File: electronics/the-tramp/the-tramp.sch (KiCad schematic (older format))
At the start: 14 parts

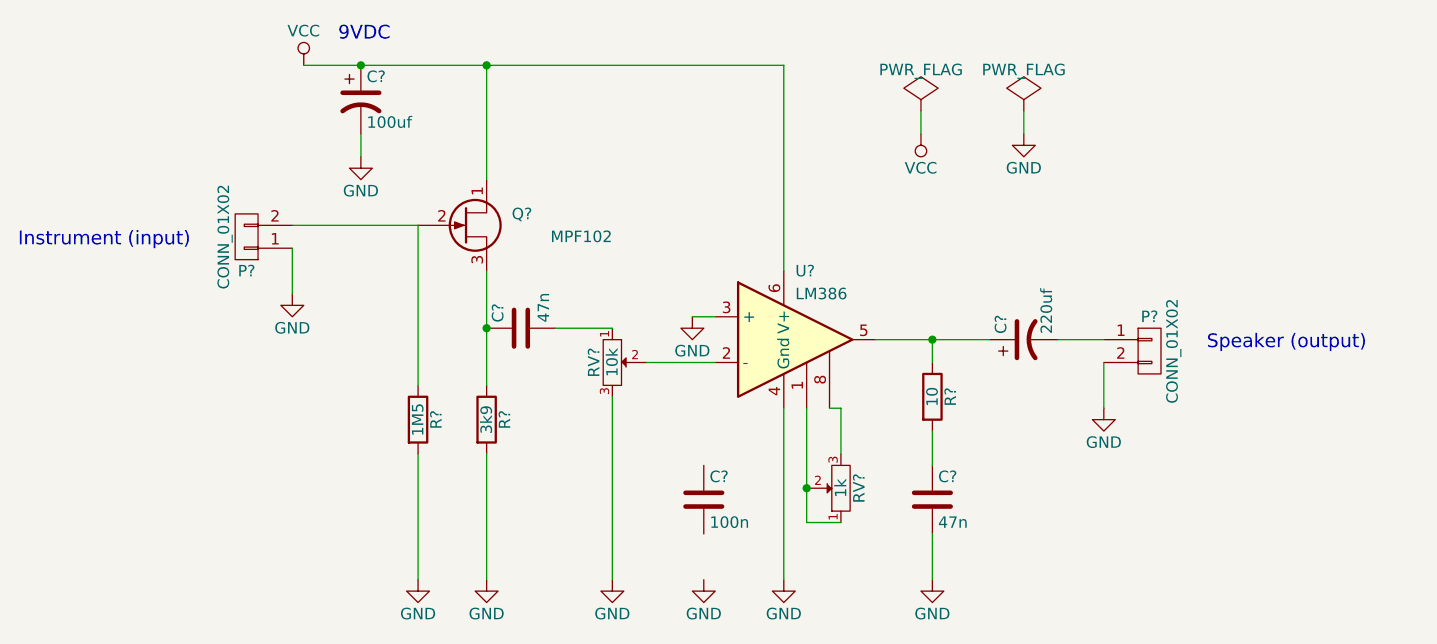
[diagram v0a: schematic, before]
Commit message: Made a custom LM386 that includes pin 7.
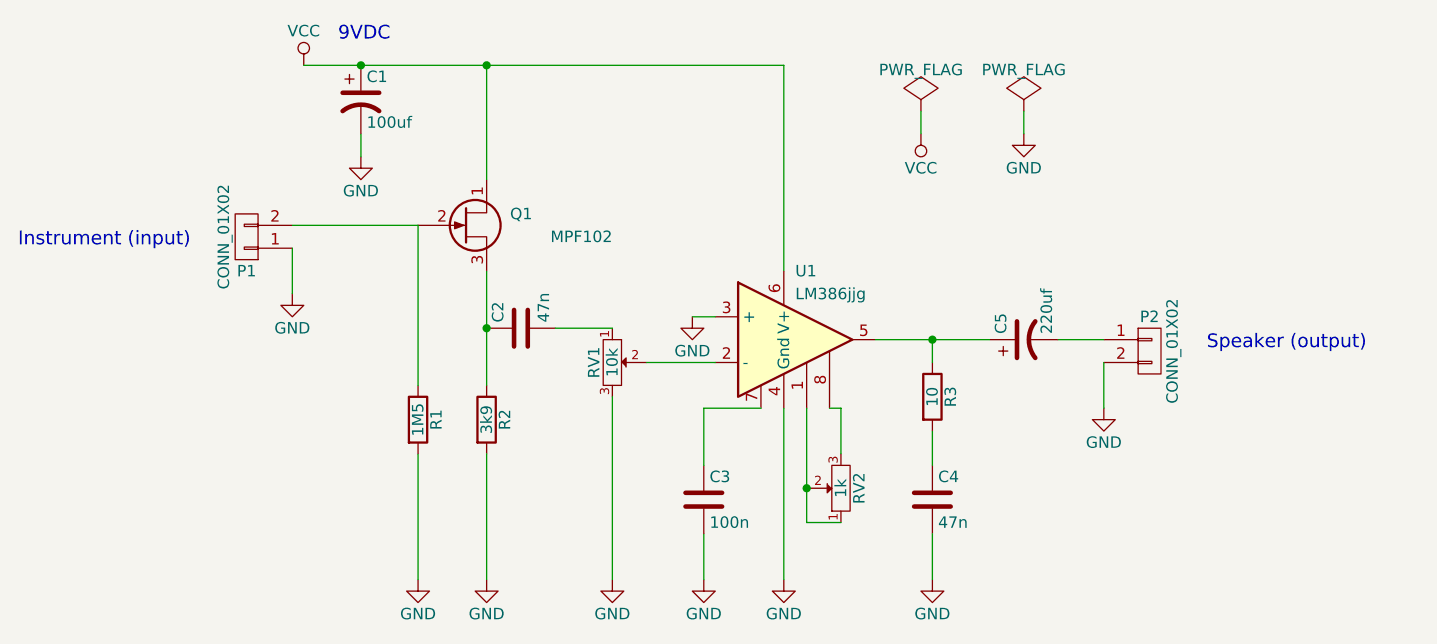
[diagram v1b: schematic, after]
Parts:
- removed U?: LM386, symbol LM386
- added U1: LM386jjg, symbol LM386jjg
- gave numbers to parts that had none: 13
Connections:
- net GND: now also C3.2, U1.3 (+), U1.4 (Gnd)
- net VCC: now also U1.6 (V+)
- net at RV2.1, RV2.2: now also U1.1
- net at RV1.2: now also U1.2 (-)
- net at C5.1, R3.1: now also U1.5
- net at RV2.3: now also U1.8
- net at C3.1: now also U1.7
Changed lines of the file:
@@
 LIBS:contrib
 LIBS:valves
-LIBS:myLib
+LIBS:tramp
 LIBS:the-tramp-cache
 EELAYER 25 0
@@
 $EndDescr
 $Comp
-L CP1 C?
+L CP1 C5
 U 1 1 5AD9FF9B
 P 6400 3700
-F 0 "C?" H 6425 3800 50  0000 L CNN
+F 0 "C5" H 6425 3800 50  0000 L CNN
 F 1 "220uf" H 6425 3600 50  0000 L CNN
 F 2 "" H 6400 3700 50  0000 C CNN
@@
 $EndComp
 $Comp
-L CP1 C?
+L CP1 C1
 U 1 1 5AD9FFC6
 P 3500 2650
-F 0 "C?" H 3525 2750 50  0000 L CNN
+F 0 "C1" H 3525 2750 50  0000 L CNN
 F 1 "100uf" H 3525 2550 50  0000 L CNN
 F 2 "" H 3500 2650 50  0000 C CNN
@@
 $EndComp
 $Comp
-L C C?
+L C C2
 U 1 1 5ADA00BD
 P 4200 3650
-F 0 "C?" H 4225 3750 50  0000 L CNN
+F 0 "C2" H 4225 3750 50  0000 L CNN
 F 1 "47n" H 4225 3550 50  0000 L CNN
 F 2 "" H 4238 3500 50  0000 C CNN
@@
 $EndComp
 $Comp
-L R R?
+L R R3
 U 1 1 5ADA0106
 P 6000 3950
-F 0 "R?" V 6080 3950 50  0000 C CNN
+F 0 "R3" V 6080 3950 50  0000 C CNN
 F 1 "10" V 6000 3950 50  0000 C CNN
 F 2 "" V 5930 3950 50  0000 C CNN
@@
 $EndComp
 $Comp
-L R R?
+L R R2
 U 1 1 5ADA0142
 P 4050 4050
-F 0 "R?" V 4130 4050 50  0000 C CNN
+F 0 "R2" V 4130 4050 50  0000 C CNN
 F 1 "3k9" V 4050 4050 50  0000 C CNN
 F 2 "" V 3980 4050 50  0000 C CNN
@@
 $EndComp
 $Comp
-L R R?
+L R R1
 U 1 1 5ADA01A6
 P 3750 4050
-F 0 "R?" V 3830 4050 50  0000 C CNN
+F 0 "R1" V 3830 4050 50  0000 C CNN
 F 1 "1M5" V 3750 4050 50  0000 C CNN
 F 2 "" V 3680 4050 50  0000 C CNN
@@
 $EndComp
 $Comp
-L POT RV?
+L POT RV1
 U 1 1 5ADA01D4
 P 4600 3800
-F 0 "RV?" H 4600 3720 50  0000 C CNN
+F 0 "RV1" H 4600 3720 50  0000 C CNN
 F 1 "10k" H 4600 3800 50  0000 C CNN
 F 2 "" H 4600 3800 50  0000 C CNN
@@
 $EndComp
 $Comp
-L POT RV?
+L POT RV2
 U 1 1 5ADA0201
 P 5600 4350
-F 0 "RV?" H 5600 4270 50  0000 C CNN
+F 0 "RV2" H 5600 4270 50  0000 C CNN
 F 1 "1k" H 5600 4350 50  0000 C CNN
 F 2 "" H 5600 4350 50  0000 C CNN
@@
 $EndComp
 $Comp
-L C C?
+L C C3
 U 1 1 5ADA025A
 P 5000 4400
-F 0 "C?" H 5025 4500 50  0000 L CNN
+F 0 "C3" H 5025 4500 50  0000 L CNN
 F 1 "100n" H 5025 4300 50  0000 L CNN
 F 2 "" H 5038 4250 50  0000 C CNN
@@
 $EndComp
 $Comp
-L Q_NJFET_DGS Q?
+L Q_NJFET_DGS Q1
 U 1 1 5ADA02C2
 P 3950 3200
-F 0 "Q?" H 4250 3250 50  0000 R CNN
+F 0 "Q1" H 4250 3250 50  0000 R CNN
 F 1 "MPF102" H 4600 3150 50  0000 R CNN
 F 2 "" H 4150 3300 50  0000 C CNN
@@
 $EndComp
 $Comp
-L C C?
+L C C4
 U 1 1 5ADA0C34
 P 6000 4400
-F 0 "C?" H 6025 4500 50  0000 L CNN
+F 0 "C4" H 6025 4500 50  0000 L CNN
 F 1 "47n" H 6025 4300 50  0000 L CNN
 F 2 "" H 6038 4250 50  0000 C CNN
@@
 $EndComp
 $Comp
-L VCC #PWR?
+L VCC #PWR2
 U 1 1 5ADA17B8
 P 3250 2500
-F 0 "#PWR?" H 3250 2350 50  0001 C CNN
+F 0 "#PWR2" H 3250 2350 50  0001 C CNN
 F 1 "VCC" H 3250 2650 50  0000 C CNN
 F 2 "" H 3250 2500 50  0000 C CNN
@@
 $EndComp
 $Comp
-L GND #PWR?
+L GND #PWR4
 U 1 1 5ADA17E4
 P 3750 4750
-F 0 "#PWR?" H 3750 4500 50  0001 C CNN
+F 0 "#PWR4" H 3750 4500 50  0001 C CNN
 F 1 "GND" H 3750 4600 50  0000 C CNN
 F 2 "" H 3750 4750 50  0000 C CNN
@@
 $EndComp
 $Comp
-L GND #PWR?
+L GND #PWR5
 U 1 1 5ADA181A
 P 4050 4750
-F 0 "#PWR?" H 4050 4500 50  0001 C CNN
+F 0 "#PWR5" H 4050 4500 50  0001 C CNN
 F 1 "GND" H 4050 4600 50  0000 C CNN
 F 2 "" H 4050 4750 50  0000 C CNN
@@
 $EndComp
 $Comp
-L GND #PWR?
+L GND #PWR8
 U 1 1 5ADA1849
 P 5000 4750
-F 0 "#PWR?" H 5000 4500 50  0001 C CNN
+F 0 "#PWR8" H 5000 4500 50  0001 C CNN
 F 1 "GND" H 5000 4600 50  0000 C CNN
 F 2 "" H 5000 4750 50  0000 C CNN
@@
 $EndComp
 $Comp
-L GND #PWR?
+L GND #PWR9
 U 1 1 5ADA1AB8
 P 5350 4750
-F 0 "#PWR?" H 5350 4500 50  0001 C CNN
+F 0 "#PWR9" H 5350 4500 50  0001 C CNN
 F 1 "GND" H 5350 4600 50  0000 C CNN
 F 2 "" H 5350 4750 50  0000 C CNN
@@
 $EndComp
 $Comp
-L GND #PWR?
+L GND #PWR11
 U 1 1 5ADA1AE7
 P 6000 4750
-F 0 "#PWR?" H 6000 4500 50  0001 C CNN
+F 0 "#PWR11" H 6000 4500 50  0001 C CNN
 F 1 "GND" H 6000 4600 50  0000 C CNN
 F 2 "" H 6000 4750 50  0000 C CNN
@@
 $EndComp
 $Comp
-L GND #PWR?
+L GND #PWR13
 U 1 1 5ADA1B16
 P 6750 4000
-F 0 "#PWR?" H 6750 3750 50  0001 C CNN
+F 0 "#PWR13" H 6750 3750 50  0001 C CNN
 F 1 "GND" H 6750 3850 50  0000 C CNN
 F 2 "" H 6750 4000 50  0000 C CNN
@@
 $EndComp
 $Comp
-L GND #PWR?
+L GND #PWR3
 U 1 1 5ADA1DC1
 P 3500 2900
-F 0 "#PWR?" H 3500 2650 50  0001 C CNN
+F 0 "#PWR3" H 3500 2650 50  0001 C CNN
 F 1 "GND" H 3500 2750 50  0000 C CNN
 F 2 "" H 3500 2900 50  0000 C CNN
@@
 	5050 3800 4750 3800
 $Comp
-L GND #PWR?
+L GND #PWR7
 U 1 1 5ADA210E
 P 4950 3600
-F 0 "#PWR?" H 4950 3350 50  0001 C CNN
+F 0 "#PWR7" H 4950 3350 50  0001 C CNN
 F 1 "GND" H 4950 3450 50  0000 C CNN
 F 2 "" H 4950 3600 50  0000 C CNN
@@
 	4600 3650 4350 3650
 Wire Wire Line
-	4050 3400 4050 3650
-Wire Wire Line
-	4050 3650 4050 3900
+	4050 3400 4050 3900
 Connection ~ 4050 3650
 Wire Wire Line
 	4050 4200 4050 4750
 $Comp
-L GND #PWR?
+L GND #PWR6
 U 1 1 5ADA2193
 P 4600 4750
-F 0 "#PWR?" H 4600 4500 50  0001 C CNN
+F 0 "#PWR6" H 4600 4500 50  0001 C CNN
 F 1 "GND" H 4600 4600 50  0000 C CNN
 F 2 "" H 4600 4750 50  0000 C CNN
@@
 	5350 2500 5350 3400
 Wire Wire Line
-	3250 2500 3500 2500
-Wire Wire Line
-	3500 2500 4050 2500
-Wire Wire Line
-	4050 2500 5350 2500
+	3250 2500 5350 2500
 Connection ~ 3500 2500
 Wire Wire Line
@@
 	3500 2800 3500 2900
 Wire Wire Line
-	5750 3700 6000 3700
-Wire Wire Line
-	6000 3700 6250 3700
+	5750 3700 6250 3700
 Wire Wire Line
 	6000 3800 6000 3700
@@
 	6000 4550 6000 4750
 Wire Wire Line
-	5450 4000 5450 4350
-Wire Wire Line
-	5450 4350 5450 4500
+	5450 4000 5450 4500
 Wire Wire Line
 	5450 4500 5600 4500
@@
 	5350 4000 5350 4750
 $Comp
-L CONN_01X02 P?
+L CONN_01X02 P2
 U 1 1 5ADA31D0
 P 6950 3750
-F 0 "P?" H 6950 3900 50  0000 C CNN
+F 0 "P2" H 6950 3900 50  0000 C CNN
 F 1 "CONN_01X02" V 7050 3750 50  0000 C CNN
 F 2 "" H 6950 3750 50  0000 C CNN
@@
 	6750 3800 6750 4000
 $Comp
-L CONN_01X02 P?
+L CONN_01X02 P1
 U 1 1 5ADA38CB
 P 3000 3250
-F 0 "P?" H 3000 3400 50  0000 C CNN
+F 0 "P1" H 3000 3400 50  0000 C CNN
 F 1 "CONN_01X02" V 3100 3250 50  0000 C CNN
 F 2 "" H 3000 3250 50  0000 C CNN
@@
 $EndComp
 $Comp
-L GND #PWR?
+L GND #PWR1
 U 1 1 5ADA3A4A
 P 3200 3500
-F 0 "#PWR?" H 3200 3250 50  0001 C CNN
+F 0 "#PWR1" H 3200 3250 50  0001 C CNN
 F 1 "GND" H 3200 3350 50  0000 C CNN
 F 2 "" H 3200 3500 50  0000 C CNN
@@
 	3200 3300 3200 3500
 $Comp
-L PWR_FLAG #FLG?
+L PWR_FLAG #FLG1
 U 1 1 5ADA4A9D
 P 5950 2700
-F 0 "#FLG?" H 5950 2795 50  0001 C CNN
+F 0 "#FLG1" H 5950 2795 50  0001 C CNN
 F 1 "PWR_FLAG" H 5950 2880 50  0000 C CNN
 F 2 "" H 5950 2700 50  0000 C CNN
@@
 $EndComp
 $Comp
-L VCC #PWR?
+L VCC #PWR10
 U 1 1 5ADA4ACD
 P 5950 2800
-F 0 "#PWR?" H 5950 2650 50  0001 C CNN
+F 0 "#PWR10" H 5950 2650 50  0001 C CNN
 F 1 "VCC" H 5950 2950 50  0000 C CNN
 F 2 "" H 5950 2800 50  0000 C CNN
@@
 $EndComp
 $Comp
-L PWR_FLAG #FLG?
+L PWR_FLAG #FLG2
 U 1 1 5ADA4B60
 P 6400 2700
-F 0 "#FLG?" H 6400 2795 50  0001 C CNN
+F 0 "#FLG2" H 6400 2795 50  0001 C CNN
 F 1 "PWR_FLAG" H 6400 2880 50  0000 C CNN
 F 2 "" H 6400 2700 50  0000 C CNN
@@
 $EndComp
 $Comp
-L GND #PWR?
+L GND #PWR12
 U 1 1 5ADA4B95
 P 6400 2800
-F 0 "#PWR?" H 6400 2550 50  0001 C CNN
+F 0 "#PWR12" H 6400 2550 50  0001 C CNN
 F 1 "GND" H 6400 2650 50  0000 C CNN
 F 2 "" H 6400 2800 50  0000 C CNN
@@
 	5600 4000 5600 4200
 $Comp
-L LM386 U?
-U 1 1 5AD9FF41
+L LM386jjg U1
+U 1 1 5ADA290D
 P 5350 3700
-F 0 "U?" H 5400 4000 50  0000 L CNN
-F 1 "LM386" H 5400 3900 50  0000 L CNN
+F 0 "U1" H 5400 4000 50  0000 L CNN
+F 1 "LM386jjg" H 5400 3900 50  0000 L CNN
 F 2 "" H 5450 3800 50  0000 C CNN
 F 3 "" H 5550 3900 50  0000 C CNN
@@
 	1    0    0    -1
 $EndComp
+Wire Wire Line
+	5250 4000 5000 4000
+Wire Wire Line
+	5000 4000 5000 4250
+Wire Wire Line
+	5000 4550 5000 4750
 $EndSCHEMATC

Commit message: First run at laying out the board.
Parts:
- C1, C5: footprint (none) -> Capacitors_ThroughHole:C_Radial_D8_L11.5_P3.5
- C2, C3, C4: footprint (none) -> Capacitors_ThroughHole:C_Rect_L7.5_W6.5_P5
- P1, P2: footprint (none) -> Pin_Headers:Pin_Header_Straight_1x02
- Q1: footprint (none) -> TO_SOT_Packages_THT:TO-92_Inline_Wide
- R1, R2, R3: footprint (none) -> Discret:R3
- RV1, RV2: footprint (none) -> Potentiometers:Potentiometer_Alps-RK16-single_largePads
- U1: footprint (none) -> Housings_DIP:DIP-8_W7.62mm_LongPads
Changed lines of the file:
@@
 F 0 "C5" H 6425 3800 50  0000 L CNN
 F 1 "220uf" H 6425 3600 50  0000 L CNN
-F 2 "" H 6400 3700 50  0000 C CNN
+F 2 "Capacitors_ThroughHole:C_Radial_D8_L11.5_P3.5" H 6400 3700 50  0001 C CNN
 F 3 "" H 6400 3700 50  0000 C CNN
 	1    6400 3700
@@
 F 0 "C1" H 3525 2750 50  0000 L CNN
 F 1 "100uf" H 3525 2550 50  0000 L CNN
-F 2 "" H 3500 2650 50  0000 C CNN
+F 2 "Capacitors_ThroughHole:C_Radial_D8_L11.5_P3.5" H 3500 2650 50  0001 C CNN
 F 3 "" H 3500 2650 50  0000 C CNN
 	1    3500 2650
@@
 F 0 "C2" H 4225 3750 50  0000 L CNN
 F 1 "47n" H 4225 3550 50  0000 L CNN
-F 2 "" H 4238 3500 50  0000 C CNN
+F 2 "Capacitors_ThroughHole:C_Rect_L7.5_W6.5_P5" H 4238 3500 50  0001 C CNN
 F 3 "" H 4200 3650 50  0000 C CNN
 	1    4200 3650
@@
 F 0 "R3" V 6080 3950 50  0000 C CNN
 F 1 "10" V 6000 3950 50  0000 C CNN
-F 2 "" V 5930 3950 50  0000 C CNN
+F 2 "Discret:R3" V 5930 3950 50  0001 C CNN
 F 3 "" H 6000 3950 50  0000 C CNN
 	1    6000 3950
@@
 F 0 "R2" V 4130 4050 50  0000 C CNN
 F 1 "3k9" V 4050 4050 50  0000 C CNN
-F 2 "" V 3980 4050 50  0000 C CNN
+F 2 "Discret:R3" V 3980 4050 50  0001 C CNN
 F 3 "" H 4050 4050 50  0000 C CNN
 	1    4050 4050
@@
 F 0 "R1" V 3830 4050 50  0000 C CNN
 F 1 "1M5" V 3750 4050 50  0000 C CNN
-F 2 "" V 3680 4050 50  0000 C CNN
+F 2 "Discret:R3" V 3680 4050 50  0001 C CNN
 F 3 "" H 3750 4050 50  0000 C CNN
 	1    3750 4050
@@
 F 0 "RV1" H 4600 3720 50  0000 C CNN
 F 1 "10k" H 4600 3800 50  0000 C CNN
-F 2 "" H 4600 3800 50  0000 C CNN
+F 2 "Potentiometers:Potentiometer_Alps-RK16-single_largePads" H 4600 3800 50  0001 C CNN
 F 3 "" H 4600 3800 50  0000 C CNN
 	1    4600 3800
@@
 F 0 "RV2" H 5600 4270 50  0000 C CNN
 F 1 "1k" H 5600 4350 50  0000 C CNN
-F 2 "" H 5600 4350 50  0000 C CNN
+F 2 "Potentiometers:Potentiometer_Alps-RK16-single_largePads" H 5600 4350 50  0001 C CNN
 F 3 "" H 5600 4350 50  0000 C CNN
 	1    5600 4350
@@
 F 0 "C3" H 5025 4500 50  0000 L CNN
 F 1 "100n" H 5025 4300 50  0000 L CNN
-F 2 "" H 5038 4250 50  0000 C CNN
+F 2 "Capacitors_ThroughHole:C_Rect_L7.5_W6.5_P5" H 5038 4250 50  0001 C CNN
 F 3 "" H 5000 4400 50  0000 C CNN
 	1    5000 4400
@@
 F 0 "Q1" H 4250 3250 50  0000 R CNN
 F 1 "MPF102" H 4600 3150 50  0000 R CNN
-F 2 "" H 4150 3300 50  0000 C CNN
+F 2 "TO_SOT_Packages_THT:TO-92_Inline_Wide" H 4150 3300 50  0001 C CNN
 F 3 "" H 3950 3200 50  0000 C CNN
 	1    3950 3200
@@
 F 0 "C4" H 6025 4500 50  0000 L CNN
 F 1 "47n" H 6025 4300 50  0000 L CNN
-F 2 "" H 6038 4250 50  0000 C CNN
+F 2 "Capacitors_ThroughHole:C_Rect_L7.5_W6.5_P5" H 6038 4250 50  0001 C CNN
 F 3 "" H 6000 4400 50  0000 C CNN
 	1    6000 4400
@@
 $EndComp
 $Comp
-L VCC #PWR2
+L VCC #PWR01
 U 1 1 5ADA17B8
 P 3250 2500
-F 0 "#PWR2" H 3250 2350 50  0001 C CNN
+F 0 "#PWR01" H 3250 2350 50  0001 C CNN
 F 1 "VCC" H 3250 2650 50  0000 C CNN
 F 2 "" H 3250 2500 50  0000 C CNN
@@
 $EndComp
 $Comp
-L GND #PWR4
+L GND #PWR02
 U 1 1 5ADA17E4
 P 3750 4750
-F 0 "#PWR4" H 3750 4500 50  0001 C CNN
+F 0 "#PWR02" H 3750 4500 50  0001 C CNN
 F 1 "GND" H 3750 4600 50  0000 C CNN
 F 2 "" H 3750 4750 50  0000 C CNN
@@
 $EndComp
 $Comp
-L GND #PWR5
+L GND #PWR03
 U 1 1 5ADA181A
 P 4050 4750
-F 0 "#PWR5" H 4050 4500 50  0001 C CNN
+F 0 "#PWR03" H 4050 4500 50  0001 C CNN
 F 1 "GND" H 4050 4600 50  0000 C CNN
 F 2 "" H 4050 4750 50  0000 C CNN
@@
 $EndComp
 $Comp
-L GND #PWR8
+L GND #PWR04
 U 1 1 5ADA1849
 P 5000 4750
-F 0 "#PWR8" H 5000 4500 50  0001 C CNN
+F 0 "#PWR04" H 5000 4500 50  0001 C CNN
 F 1 "GND" H 5000 4600 50  0000 C CNN
 F 2 "" H 5000 4750 50  0000 C CNN
@@
 $EndComp
 $Comp
-L GND #PWR9
+L GND #PWR05
 U 1 1 5ADA1AB8
 P 5350 4750
-F 0 "#PWR9" H 5350 4500 50  0001 C CNN
+F 0 "#PWR05" H 5350 4500 50  0001 C CNN
 F 1 "GND" H 5350 4600 50  0000 C CNN
 F 2 "" H 5350 4750 50  0000 C CNN
@@
 $EndComp
 $Comp
-L GND #PWR11
+L GND #PWR06
 U 1 1 5ADA1AE7
 P 6000 4750
-F 0 "#PWR11" H 6000 4500 50  0001 C CNN
+F 0 "#PWR06" H 6000 4500 50  0001 C CNN
 F 1 "GND" H 6000 4600 50  0000 C CNN
 F 2 "" H 6000 4750 50  0000 C CNN
@@
 $EndComp
 $Comp
-L GND #PWR13
+L GND #PWR07
 U 1 1 5ADA1B16
 P 6750 4000
-F 0 "#PWR13" H 6750 3750 50  0001 C CNN
+F 0 "#PWR07" H 6750 3750 50  0001 C CNN
 F 1 "GND" H 6750 3850 50  0000 C CNN
 F 2 "" H 6750 4000 50  0000 C CNN
@@
 $EndComp
 $Comp
-L GND #PWR3
+L GND #PWR08
 U 1 1 5ADA1DC1
 P 3500 2900
-F 0 "#PWR3" H 3500 2650 50  0001 C CNN
+F 0 "#PWR08" H 3500 2650 50  0001 C CNN
 F 1 "GND" H 3500 2750 50  0000 C CNN
 F 2 "" H 3500 2900 50  0000 C CNN
@@
 	5050 3800 4750 3800
 $Comp
-L GND #PWR7
+L GND #PWR09
 U 1 1 5ADA210E
 P 4950 3600
-F 0 "#PWR7" H 4950 3350 50  0001 C CNN
+F 0 "#PWR09" H 4950 3350 50  0001 C CNN
 F 1 "GND" H 4950 3450 50  0000 C CNN
 F 2 "" H 4950 3600 50  0000 C CNN
@@
 	4050 4200 4050 4750
 $Comp
-L GND #PWR6
+L GND #PWR010
 U 1 1 5ADA2193
 P 4600 4750
-F 0 "#PWR6" H 4600 4500 50  0001 C CNN
+F 0 "#PWR010" H 4600 4500 50  0001 C CNN
 F 1 "GND" H 4600 4600 50  0000 C CNN
 F 2 "" H 4600 4750 50  0000 C CNN
@@
 F 0 "P2" H 6950 3900 50  0000 C CNN
 F 1 "CONN_01X02" V 7050 3750 50  0000 C CNN
-F 2 "" H 6950 3750 50  0000 C CNN
+F 2 "Pin_Headers:Pin_Header_Straight_1x02" H 6950 3750 50  0001 C CNN
 F 3 "" H 6950 3750 50  0000 C CNN
 	1    6950 3750
@@
 F 0 "P1" H 3000 3400 50  0000 C CNN
 F 1 "CONN_01X02" V 3100 3250 50  0000 C CNN
-F 2 "" H 3000 3250 50  0000 C CNN
+F 2 "Pin_Headers:Pin_Header_Straight_1x02" H 3000 3250 50  0001 C CNN
 F 3 "" H 3000 3250 50  0000 C CNN
 	1    3000 3250
@@
 $EndComp
 $Comp
-L GND #PWR1
+L GND #PWR011
 U 1 1 5ADA3A4A
 P 3200 3500
-F 0 "#PWR1" H 3200 3250 50  0001 C CNN
+F 0 "#PWR011" H 3200 3250 50  0001 C CNN
 F 1 "GND" H 3200 3350 50  0000 C CNN
 F 2 "" H 3200 3500 50  0000 C CNN
@@
 	3200 3300 3200 3500
 $Comp
-L PWR_FLAG #FLG1
+L PWR_FLAG #FLG012
 U 1 1 5ADA4A9D
 P 5950 2700
-F 0 "#FLG1" H 5950 2795 50  0001 C CNN
+F 0 "#FLG012" H 5950 2795 50  0001 C CNN
 F 1 "PWR_FLAG" H 5950 2880 50  0000 C CNN
 F 2 "" H 5950 2700 50  0000 C CNN
@@
 $EndComp
 $Comp
-L VCC #PWR10
+L VCC #PWR013
 U 1 1 5ADA4ACD
 P 5950 2800
-F 0 "#PWR10" H 5950 2650 50  0001 C CNN
+F 0 "#PWR013" H 5950 2650 50  0001 C CNN
 F 1 "VCC" H 5950 2950 50  0000 C CNN
 F 2 "" H 5950 2800 50  0000 C CNN
@@
 $EndComp
 $Comp
-L PWR_FLAG #FLG2
+L PWR_FLAG #FLG014
 U 1 1 5ADA4B60
 P 6400 2700
-F 0 "#FLG2" H 6400 2795 50  0001 C CNN
+F 0 "#FLG014" H 6400 2795 50  0001 C CNN
 F 1 "PWR_FLAG" H 6400 2880 50  0000 C CNN
 F 2 "" H 6400 2700 50  0000 C CNN
@@
 $EndComp
 $Comp
-L GND #PWR12
+L GND #PWR015
 U 1 1 5ADA4B95
 P 6400 2800
-F 0 "#PWR12" H 6400 2550 50  0001 C CNN
+F 0 "#PWR015" H 6400 2550 50  0001 C CNN
 F 1 "GND" H 6400 2650 50  0000 C CNN
 F 2 "" H 6400 2800 50  0000 C CNN
@@
 F 0 "U1" H 5400 4000 50  0000 L CNN
 F 1 "LM386jjg" H 5400 3900 50  0000 L CNN
-F 2 "" H 5450 3800 50  0000 C CNN
+F 2 "Housings_DIP:DIP-8_W7.62mm_LongPads" H 5450 3800 50  0001 C CNN
 F 3 "" H 5550 3900 50  0000 C CNN
 	1    5350 3700

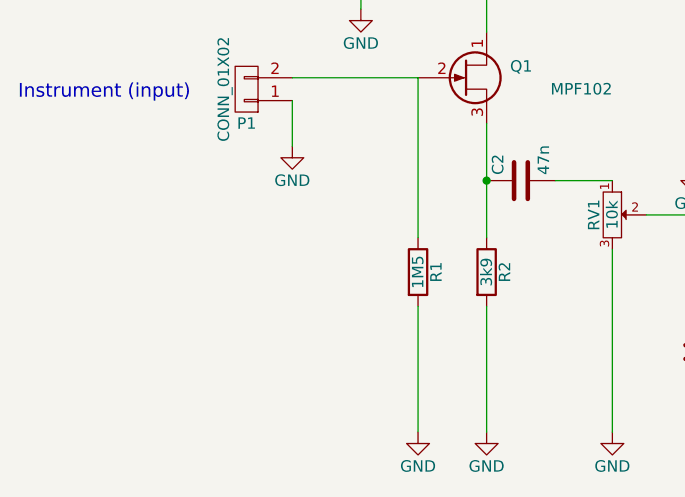
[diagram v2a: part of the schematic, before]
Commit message: Added power connector and copper fills.
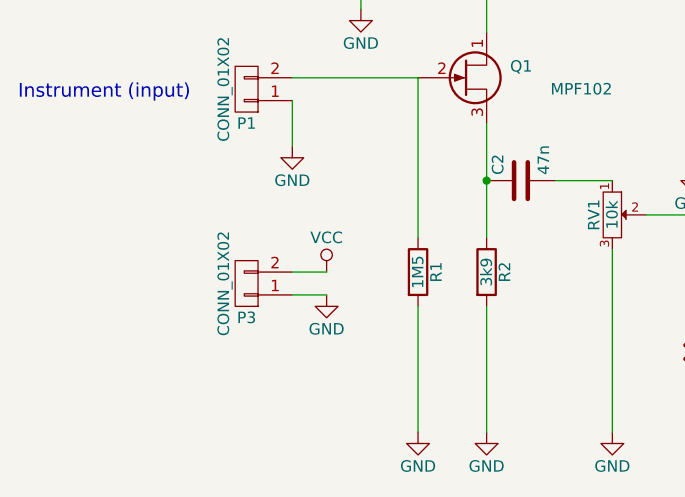
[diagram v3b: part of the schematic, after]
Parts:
- added P3: CONN_01X02, Pin_Headers:Pin_Header_Straight_1x02, symbol CONN_01X02
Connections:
- net GND: now also P3.1 (P1)
- net VCC: now also P3.2 (P2)
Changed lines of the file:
@@
 Wire Wire Line
 	5000 4550 5000 4750
+$Comp
+L CONN_01X02 P3
+U 1 1 5ADA43FD
+P 3000 4100
+F 0 "P3" H 3000 4250 50  0000 C CNN
+F 1 "CONN_01X02" V 3100 4100 50  0000 C CNN
+F 2 "Pin_Headers:Pin_Header_Straight_1x02" H 3000 4100 50  0001 C CNN
+F 3 "" H 3000 4100 50  0000 C CNN
+	1    3000 4100
+	-1   0    0    1
+$EndComp
+$Comp
+L VCC #PWR016
+U 1 1 5ADA4496
+P 3350 4050
+F 0 "#PWR016" H 3350 3900 50  0001 C CNN
+F 1 "VCC" H 3350 4200 50  0000 C CNN
+F 2 "" H 3350 4050 50  0000 C CNN
+F 3 "" H 3350 4050 50  0000 C CNN
+	1    3350 4050
+	1    0    0    -1
+$EndComp
+$Comp
+L GND #PWR017
+U 1 1 5ADA44C8
+P 3350 4150
+F 0 "#PWR017" H 3350 3900 50  0001 C CNN
+F 1 "GND" H 3350 4000 50  0000 C CNN
+F 2 "" H 3350 4150 50  0000 C CNN
+F 3 "" H 3350 4150 50  0000 C CNN
+	1    3350 4150
+	1    0    0    -1
+$EndComp
+Wire Wire Line
+	3200 4050 3350 4050
+Wire Wire Line
+	3200 4150 3350 4150
 $EndSCHEMATC
